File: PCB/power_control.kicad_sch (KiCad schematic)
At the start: 10 parts

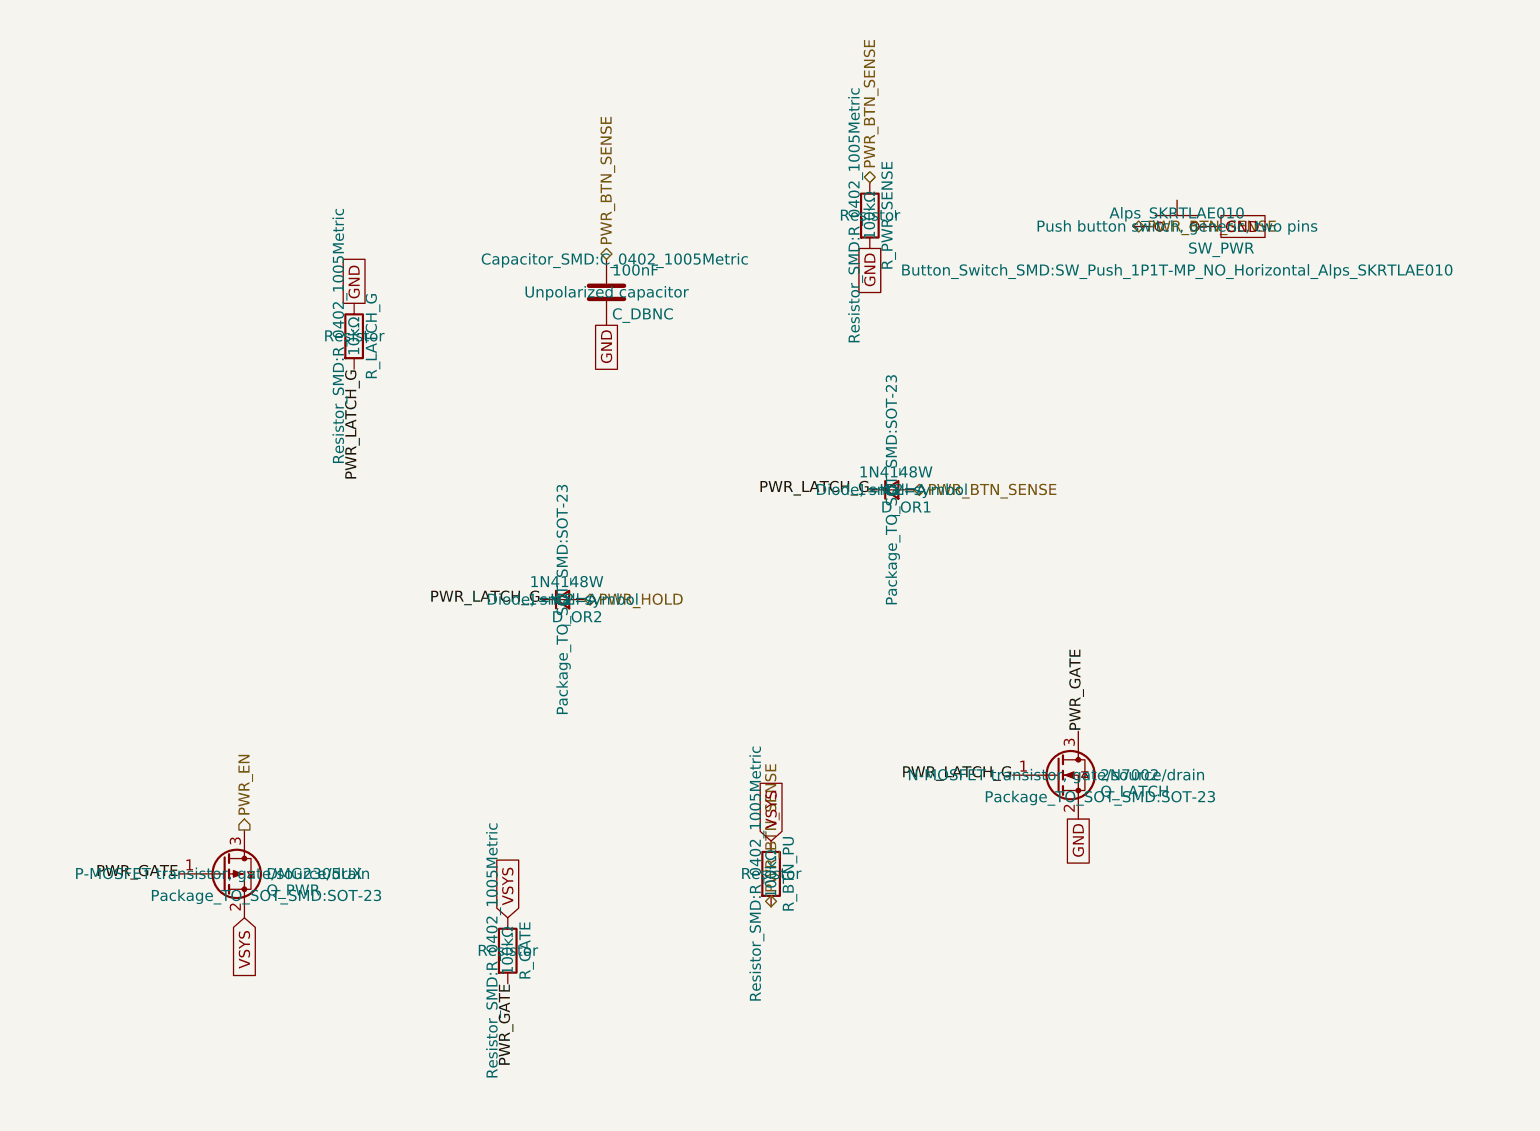
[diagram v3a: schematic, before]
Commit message: layout: everything is on the board
The board edge cuts are down to 100mm x 35mm. All the components have the right footprints and are on the board, but no traces exist yet, and not all circuits are laid out properly yet. Lots of DRC warnings.
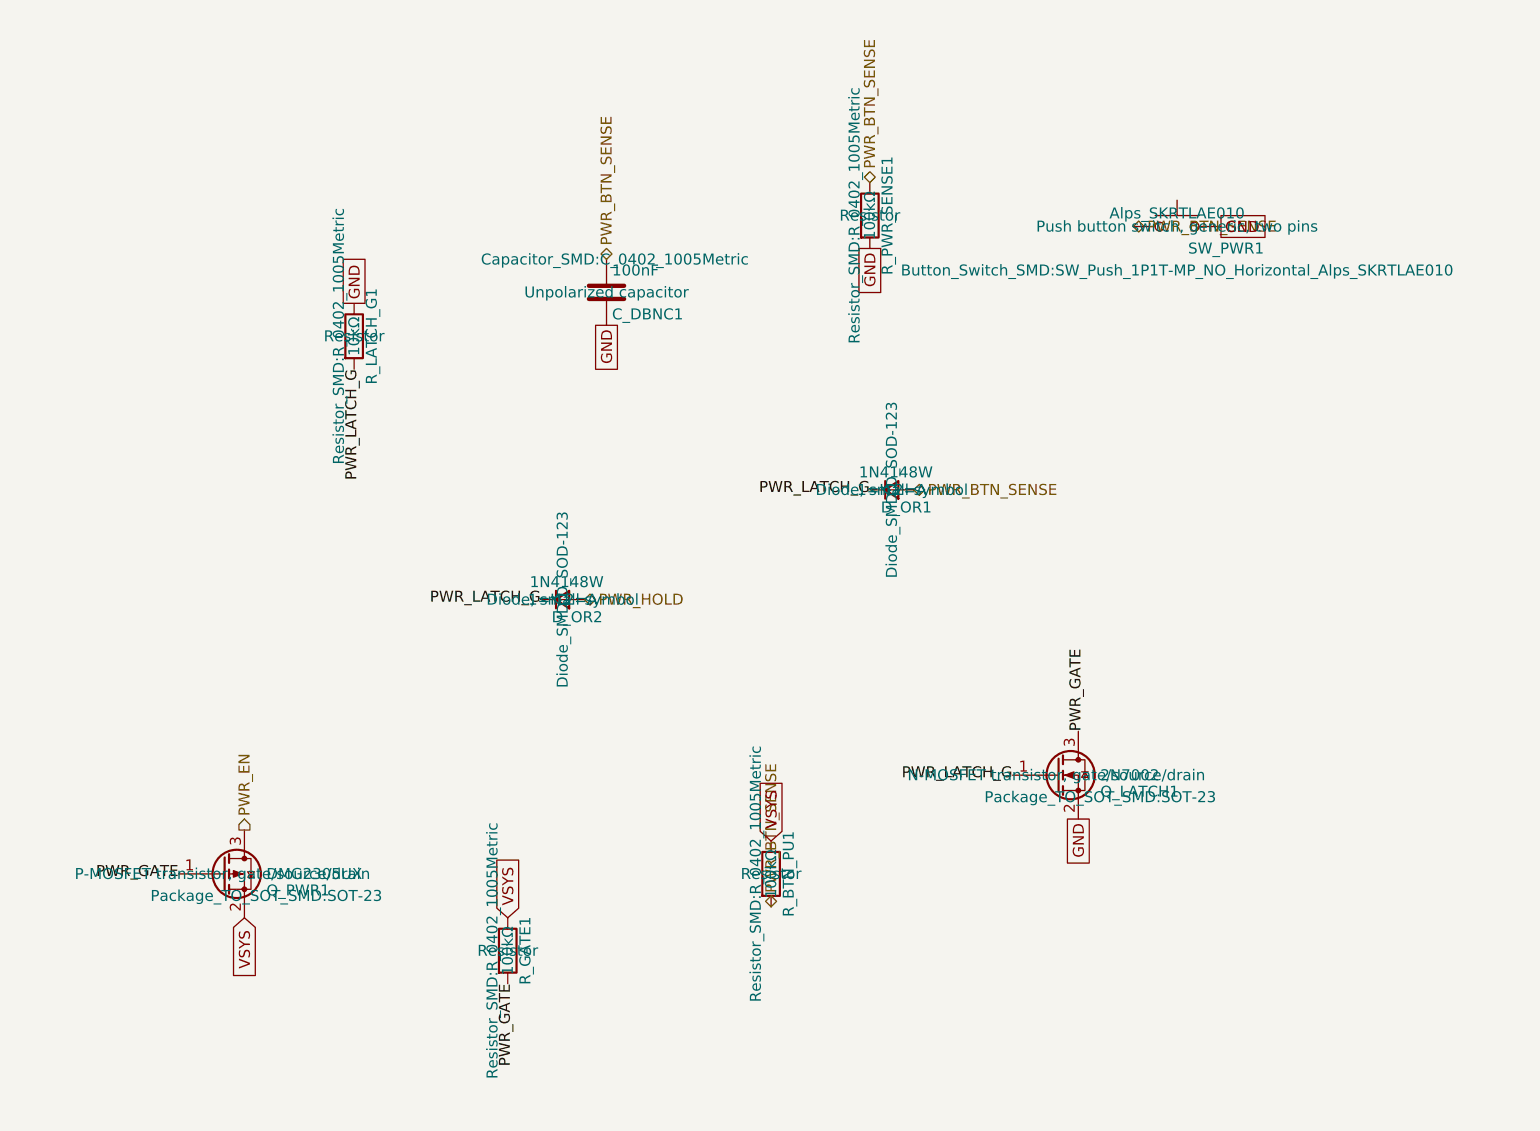
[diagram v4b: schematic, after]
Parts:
- removed C_DBNC: 100nF, Capacitor_SMD:C_0402_1005Metric, symbol Device:C
- removed Q_LATCH: 2N7002, Package_TO_SOT_SMD:SOT-23, symbol Transistor_FET:Q_NMOS_GSD
- removed Q_PWR: DMG2305UX, Package_TO_SOT_SMD:SOT-23, symbol Transistor_FET:Q_PMOS_GSD
- removed R_BTN_PU, R_GATE, R_PWR_SENSE: 100kΩ, Resistor_SMD:R_0402_1005Metric, symbol Device:R
- removed R_LATCH_G: 10kΩ, Resistor_SMD:R_0402_1005Metric, symbol Device:R
- removed SW_PWR: Alps_SKRTLAE010, Button_Switch_SMD:SW_Push_1P1T-MP_NO_Horizontal_Alps_SKRTLAE010, symbol Switch:SW_Push
- added C_DBNC1: 100nF, Capacitor_SMD:C_0402_1005Metric, symbol Device:C
- added Q_LATCH1: 2N7002, Package_TO_SOT_SMD:SOT-23, symbol Transistor_FET:Q_NMOS_GSD
- added Q_PWR1: DMG2305UX, Package_TO_SOT_SMD:SOT-23, symbol Transistor_FET:Q_PMOS_GSD
- added R_BTN_PU1, R_GATE1, R_PWR_SENSE1: 100kΩ, Resistor_SMD:R_0402_1005Metric, symbol Device:R
- added R_LATCH_G1: 10kΩ, Resistor_SMD:R_0402_1005Metric, symbol Device:R
- added SW_PWR1: Alps_SKRTLAE010, Button_Switch_SMD:SW_Push_1P1T-MP_NO_Horizontal_Alps_SKRTLAE010, symbol Switch:SW_Push
- D_OR1, D_OR2: footprint Package_TO_SOT_SMD:SOT-23 -> Diode_SMD:D_SOD-123
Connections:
- net GND: now also C_DBNC1.2, Q_LATCH1.2 (S), R_LATCH_G1.1, R_PWR_SENSE1.2, SW_PWR1.2
- net PWR_BTN_SENSE: now also C_DBNC1.1, R_BTN_PU1.2, R_PWR_SENSE1.1, SW_PWR1.1
- net PWR_EN: now also Q_PWR1.3 (D)
- net PWR_GATE: now also Q_LATCH1.3 (D), Q_PWR1.1 (G), R_GATE1.2
- net PWR_LATCH_G: now also Q_LATCH1.1 (G), R_LATCH_G1.2
- net VSYS: now also Q_PWR1.2 (S), R_BTN_PU1.1, R_GATE1.1

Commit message: task: part number populated (#26)
kicad-happy run part 2 - MPN numbers populated
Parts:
- C_DBNC1: MF (none) -> Yageo; Manufacturer_Part_Number (none) -> CC0402KRX7R9BB104
- D_OR1, D_OR2: MF (none) -> Diodes Incorporated; Manufacturer_Part_Number (none) -> 1N4148W-7-F
- Q_LATCH1: MF (none) -> onsemi; Manufacturer_Part_Number (none) -> 2N7002LT1G
- Q_PWR1: MF (none) -> Diodes Incorporated; Manufacturer_Part_Number (none) -> DMG2305UX-7
- R_BTN_PU1, R_GATE1, R_PWR_SENSE1: MF (none) -> Yageo; Manufacturer_Part_Number (none) -> RC0402FR-07100KL
- R_LATCH_G1: MF (none) -> Yageo; Manufacturer_Part_Number (none) -> RC0402FR-0710KL
- SW_PWR1: MF (none) -> Alps Alpine; Manufacturer_Part_Number (none) -> SKRTLAE010
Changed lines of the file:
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@@
+			)
+		)
+		(property "MF" "Yageo" (at 0 0 0)
+			(effects
+				(font
+					(size 1.27 1.27)
+				)
+				(hide yes)
+			)
+		)
+		(property "Manufacturer_Part_Number" "CC0402KRX7R9BB104" (at 0 0 0)
+			(effects
+				(font
+					(size 1.27 1.27)
+				)
+				(hide yes)
 			)
 		)
@@
 			)
 		)
+		(property "MF" "Alps Alpine" (at 0 0 0)
+			(effects
+				(font
+					(size 1.27 1.27)
+				)
+				(hide yes)
+			)
+		)
+		(property "Manufacturer_Part_Number" "SKRTLAE010" (at 0 0 0)
+			(effects
+				(font
+					(size 1.27 1.27)
+				)
+				(hide yes)
+			)
+		)
 		(pin "1"
 		)
@@
 			)
 		)
+		(property "MF" "Diodes Incorporated" (at 0 0 0)
+			(effects
+				(font
+					(size 1.27 1.27)
+				)
+				(hide yes)
+			)
+		)
+		(property "Manufacturer_Part_Number" "DMG2305UX-7" (at 0 0 0)
+			(effects
+				(font
+					(size 1.27 1.27)
+				)
+				(hide yes)
+			)
+		)
 		(pin "1"
 		)
@@
 			)
 		)
+		(property "MF" "Diodes Incorporated" (at 0 0 0)
+			(effects
+				(font
+					(size 1.27 1.27)
+				)
+				(hide yes)
+			)
+		)
+		(property "Manufacturer_Part_Number" "1N4148W-7-F" (at 0 0 0)
+			(effects
+				(font
+					(size 1.27 1.27)
+				)
+				(hide yes)
+			)
+		)
 		(pin "1"
 		)
@@
 			)
 		)
+		(property "MF" "Yageo" (at 0 0 0)
+			(effects
+				(font
+					(size 1.27 1.27)
+				)
+				(hide yes)
+			)
+		)
+		(property "Manufacturer_Part_Number" "RC0402FR-07100KL" (at 0 0 0)
+			(effects
+				(font
+					(size 1.27 1.27)
+				)
+				(hide yes)
+			)
+		)
 		(pin "1"
 		)
@@
 			)
 		)
+		(property "MF" "Yageo" (at 0 0 0)
+			(effects
+				(font
+					(size 1.27 1.27)
+				)
+				(hide yes)
+			)
+		)
+		(property "Manufacturer_Part_Number" "RC0402FR-0710KL" (at 0 0 0)
+			(effects
+				(font
+					(size 1.27 1.27)
+				)
+				(hide yes)
+			)
+		)
 		(pin "1"
 		)
@@
 			)
 		)
+		(property "MF" "Yageo" (at 0 0 0)
+			(effects
+				(font
+					(size 1.27 1.27)
+				)
+				(hide yes)
+			)
+		)
+		(property "Manufacturer_Part_Number" "RC0402FR-07100KL" (at 0 0 0)
+			(effects
+				(font
+					(size 1.27 1.27)
+				)
+				(hide yes)
+			)
+		)
 		(pin "1"
 		)
@@
 			)
 		)
+		(property "MF" "Diodes Incorporated" (at 0 0 0)
+			(effects
+				(font
+					(size 1.27 1.27)
+				)
+				(hide yes)
+			)
+		)
+		(property "Manufacturer_Part_Number" "1N4148W-7-F" (at 0 0 0)
+			(effects
+				(font
+					(size 1.27 1.27)
+				)
+				(hide yes)
+			)
+		)
 		(pin "1"
 		)
@@
 			)
 		)
+		(property "MF" "onsemi" (at 0 0 0)
+			(effects
+				(font
+					(size 1.27 1.27)
+				)
+				(hide yes)
+			)
+		)
+		(property "Manufacturer_Part_Number" "2N7002LT1G" (at 0 0 0)
+			(effects
+				(font
+					(size 1.27 1.27)
+				)
+				(hide yes)
+			)
+		)
 		(pin "1"
 		)
@@
 			)
 		)
+		(property "MF" "Yageo" (at 0 0 0)
+			(effects
+				(font
+					(size 1.27 1.27)
+				)
+				(hide yes)
+			)
+		)
+		(property "Manufacturer_Part_Number" "RC0402FR-07100KL" (at 0 0 0)
+			(effects
+				(font
+					(size 1.27 1.27)
+				)
+				(hide yes)
+			)
+		)
